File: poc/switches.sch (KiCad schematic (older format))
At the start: 37 parts

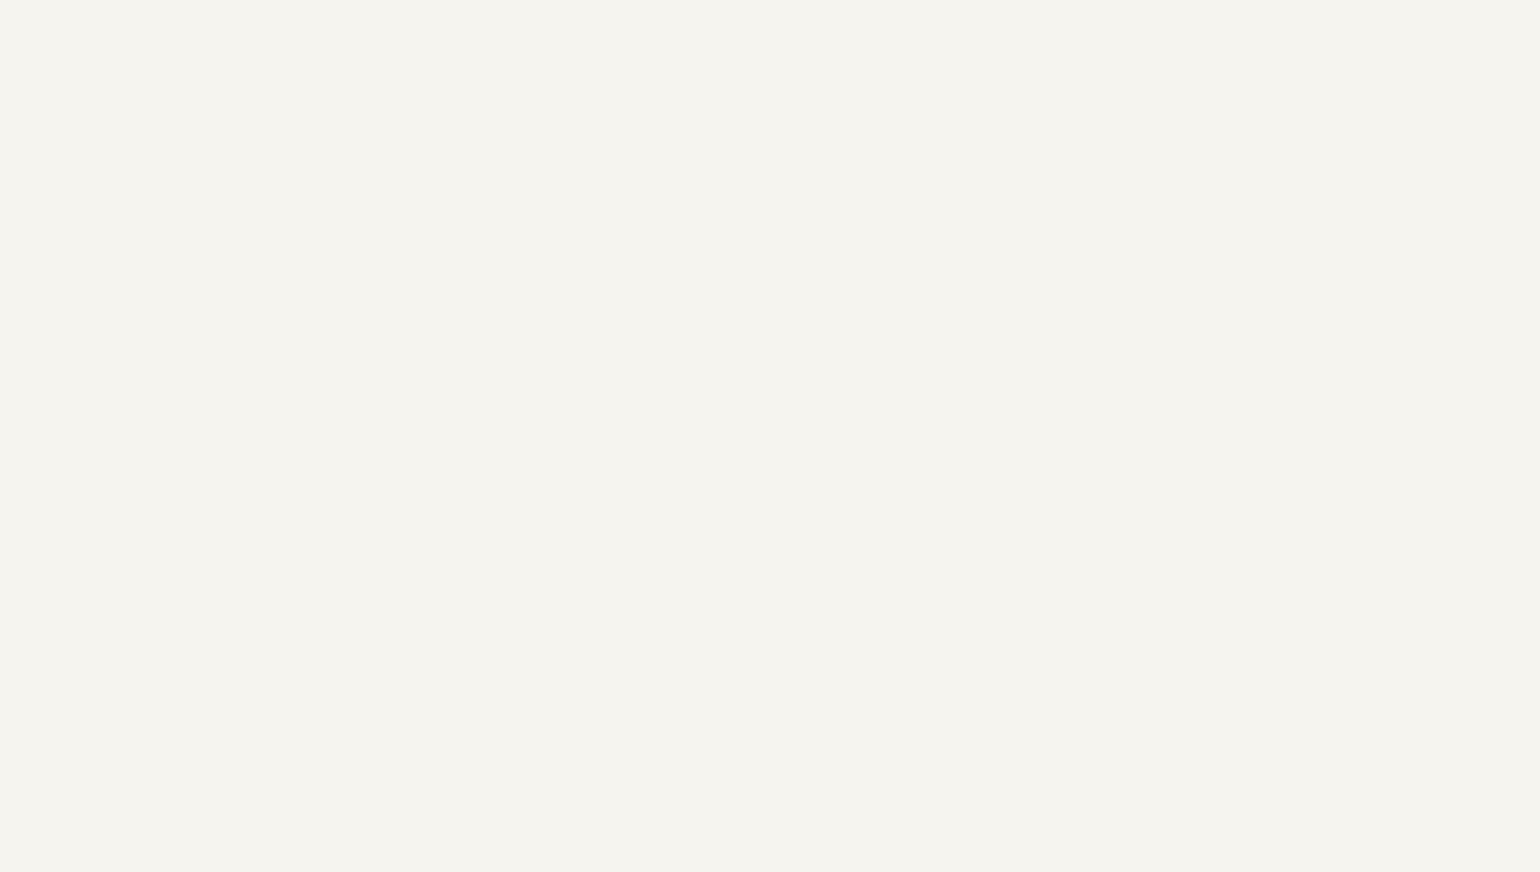
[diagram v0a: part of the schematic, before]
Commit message: Power for a gige phy
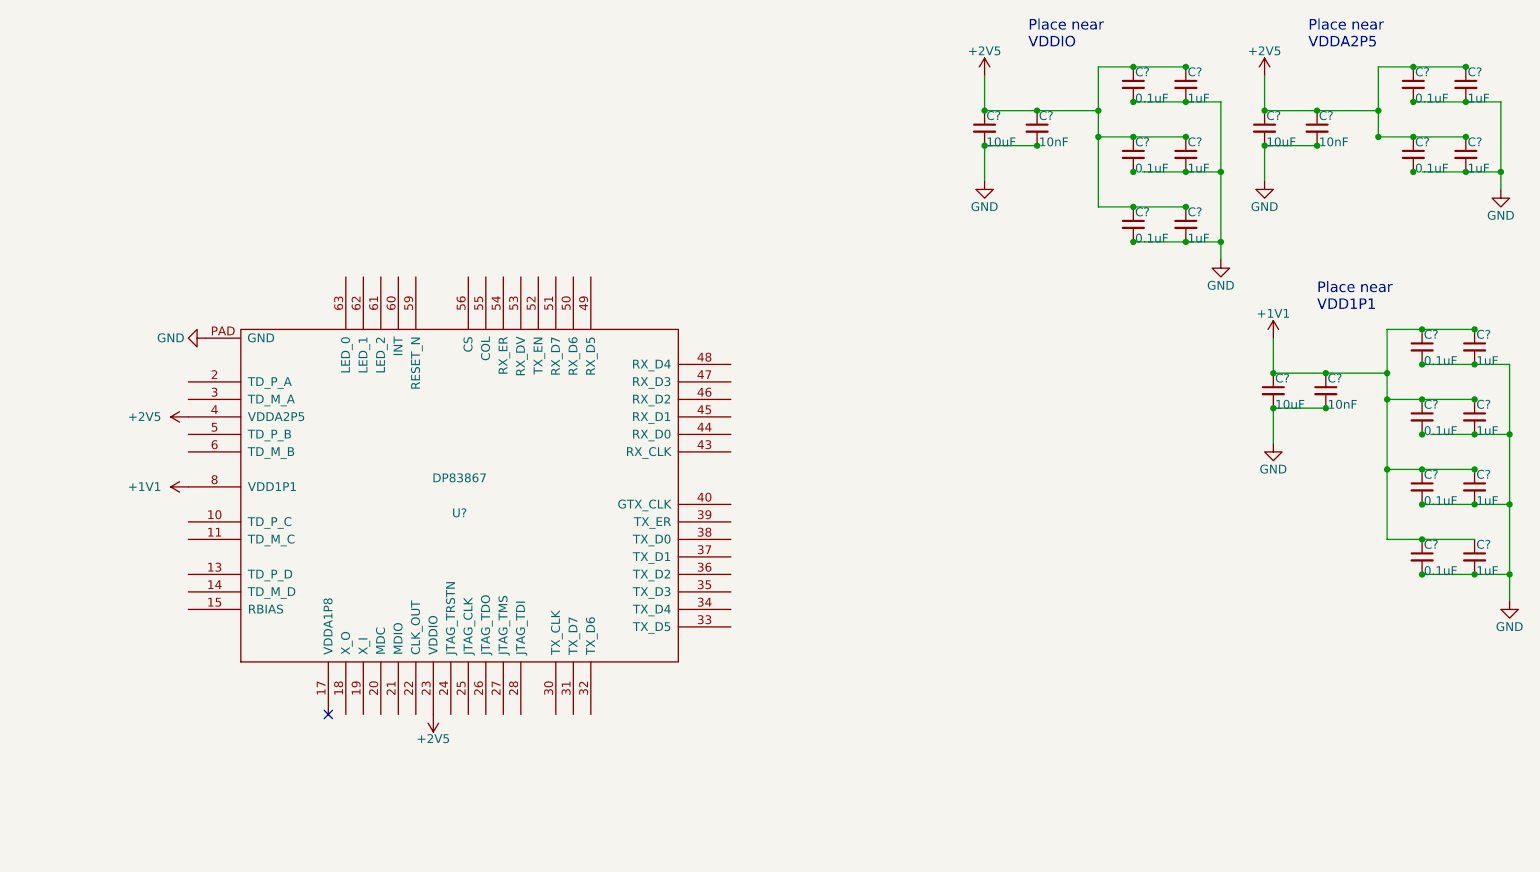
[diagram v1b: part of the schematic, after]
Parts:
- added C? (x3): 10uF, symbol C_Small
- added C? (x3): 10nF, symbol C_Small
- added C? (x9): 0.1uF, symbol C_Small
- added C? (x9): 1uF, symbol C_Small
- added U?: DP83867, MODULE, symbol DP83867
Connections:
- net labels added: +1V1
- wire segments 13 -> 49
- no-connect marks 0 -> 1
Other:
- note added: "Place near\nVDD1P1"
- note added: "Place near\nVDDA2P5"

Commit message: Further organize pi schematics; power for each chip is done!
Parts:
- added C? (x4): 0.1uF, symbol C_Small
- added R?: Belfuse_GigE, symbol Belfuse_GigE
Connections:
- wire segments 49 -> 59
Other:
- note added: "VDDA1P8 is NC\nin two power\nsupply mode"
- moved on the sheet: S?, U?
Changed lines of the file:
@@
 $Descr C 22000 17000
 encoding utf-8
-Sheet 3 3
+Sheet 2 4
 Title ""
 Date ""
@@
 L KSZ9897R S?
 U 1 1 5990AEA3
-P 7000 7250
-F 0 "S?" H 7000 7150 50  0000 C CNN
-F 1 "KSZ9897R" H 7000 7350 50  0000 C CNN
-F 2 "MODULE" H 7000 7250 50  0001 C CNN
-F 3 "DOCUMENTATION" H 7000 7250 50  0001 C CNN
-	1    7000 7250
+P 6950 7250
+F 0 "S?" H 6950 7150 50  0000 C CNN
+F 1 "KSZ9897R" H 6950 7350 50  0000 C CNN
+F 2 "MODULE" H 6950 7250 50  0001 C CNN
+F 3 "DOCUMENTATION" H 6950 7250 50  0001 C CNN
+	1    6950 7250
 	1    0    0    -1
 $EndComp
@@
 L +2V5 #PWR?
 U 1 1 5990AEB1
-P 6350 9500
-F 0 "#PWR?" H 6350 9350 50  0001 C CNN
-F 1 "+2V5" H 6350 9640 50  0000 C CNN
-F 2 "" H 6350 9500 50  0001 C CNN
-F 3 "" H 6350 9500 50  0001 C CNN
-	1    6350 9500
+P 6300 9500
+F 0 "#PWR?" H 6300 9350 50  0001 C CNN
+F 1 "+2V5" H 6300 9640 50  0000 C CNN
+F 2 "" H 6300 9500 50  0001 C CNN
+F 3 "" H 6300 9500 50  0001 C CNN
+	1    6300 9500
 	-1   0    0    1
 $EndComp
@@
 L +1V2 #PWR?
 U 1 1 5990AEB7
-P 5650 9400
-F 0 "#PWR?" H 5650 9250 50  0001 C CNN
-F 1 "+1V2" H 5650 9540 50  0000 C CNN
-F 2 "" H 5650 9400 50  0001 C CNN
-F 3 "" H 5650 9400 50  0001 C CNN
-	1    5650 9400
+P 5600 9400
+F 0 "#PWR?" H 5600 9250 50  0001 C CNN
+F 1 "+1V2" H 5600 9540 50  0000 C CNN
+F 2 "" H 5600 9400 50  0001 C CNN
+F 3 "" H 5600 9400 50  0001 C CNN
+	1    5600 9400
 	-1   0    0    1
 $EndComp
@@
 L +1V2 #PWR?
 U 1 1 5990AEBD
-P 6450 9400
-F 0 "#PWR?" H 6450 9250 50  0001 C CNN
-F 1 "+1V2" H 6450 9540 50  0000 C CNN
-F 2 "" H 6450 9400 50  0001 C CNN
-F 3 "" H 6450 9400 50  0001 C CNN
-	1    6450 9400
+P 6400 9400
+F 0 "#PWR?" H 6400 9250 50  0001 C CNN
+F 1 "+1V2" H 6400 9540 50  0000 C CNN
+F 2 "" H 6400 9400 50  0001 C CNN
+F 3 "" H 6400 9400 50  0001 C CNN
+	1    6400 9400
 	-1   0    0    1
 $EndComp
 Wire Wire Line
-	6350 9400 6350 9500
+	6300 9400 6300 9500
 $Comp
 L +2V5 #PWR?
 U 1 1 5990AEC4
-P 9350 5900
-F 0 "#PWR?" H 9350 5750 50  0001 C CNN
-F 1 "+2V5" V 9350 6100 50  0000 C CNN
-F 2 "" H 9350 5900 50  0001 C CNN
-F 3 "" H 9350 5900 50  0001 C CNN
-	1    9350 5900
+P 9300 5900
+F 0 "#PWR?" H 9300 5750 50  0001 C CNN
+F 1 "+2V5" V 9300 6100 50  0000 C CNN
+F 2 "" H 9300 5900 50  0001 C CNN
+F 3 "" H 9300 5900 50  0001 C CNN
+	1    9300 5900
 	0    1    1    0
 $EndComp
@@
 L GND #PWR?
 U 1 1 5990AECA
-P 9350 7400
-F 0 "#PWR?" H 9350 7150 50  0001 C CNN
-F 1 "GND" V 9350 7200 50  0000 C CNN
-F 2 "" H 9350 7400 50  0001 C CNN
-F 3 "" H 9350 7400 50  0001 C CNN
-	1    9350 7400
+P 9300 7400
+F 0 "#PWR?" H 9300 7150 50  0001 C CNN
+F 1 "GND" V 9300 7200 50  0000 C CNN
+F 2 "" H 9300 7400 50  0001 C CNN
+F 3 "" H 9300 7400 50  0001 C CNN
+	1    9300 7400
 	0    -1   -1   0
 $EndComp
@@
 L DP83867 U?
 U 1 1 599194AF
-P 15400 3250
-F 0 "U?" H 15400 3150 50  0000 C CNN
-F 1 "DP83867" H 15400 3350 50  0000 C CNN
-F 2 "MODULE" H 15400 3250 50  0001 C CNN
-F 3 "DOCUMENTATION" H 15400 3250 50  0001 C CNN
-	1    15400 3250
+P 13400 3200
+F 0 "U?" H 13400 3100 50  0000 C CNN
+F 1 "DP83867" H 13400 3300 50  0000 C CNN
+F 2 "MODULE" H 13400 3200 50  0001 C CNN
+F 3 "DOCUMENTATION" H 13400 3200 50  0001 C CNN
+	1    13400 3200
 	1    0    0    -1
 $EndComp
@@
 L +2V5 #PWR?
 U 1 1 5992229E
-P 15250 4500
-F 0 "#PWR?" H 15250 4350 50  0001 C CNN
-F 1 "+2V5" H 15250 4640 50  0000 C CNN
-F 2 "" H 15250 4500 50  0001 C CNN
-F 3 "" H 15250 4500 50  0001 C CNN
-	1    15250 4500
+P 13250 4450
+F 0 "#PWR?" H 13250 4300 50  0001 C CNN
+F 1 "+2V5" H 13250 4590 50  0000 C CNN
+F 2 "" H 13250 4450 50  0001 C CNN
+F 3 "" H 13250 4450 50  0001 C CNN
+	1    13250 4450
 	-1   0    0    1
 $EndComp
-NoConn ~ 14650 4500
+NoConn ~ 12650 4450
 $Comp
 L GND #PWR?
 U 1 1 59924BE1
-P 13950 2350
-F 0 "#PWR?" H 13950 2100 50  0001 C CNN
-F 1 "GND" V 13950 2150 50  0000 C CNN
-F 2 "" H 13950 2350 50  0001 C CNN
-F 3 "" H 13950 2350 50  0001 C CNN
-	1    13950 2350
+P 11950 2300
+F 0 "#PWR?" H 11950 2050 50  0001 C CNN
+F 1 "GND" V 11950 2100 50  0000 C CNN
+F 2 "" H 11950 2300 50  0001 C CNN
+F 3 "" H 11950 2300 50  0001 C CNN
+	1    11950 2300
 	0    1    1    0
 $EndComp
@@
 L +2V5 #PWR?
 U 1 1 5992579B
-P 13850 2800
-F 0 "#PWR?" H 13850 2650 50  0001 C CNN
-F 1 "+2V5" V 13850 3050 50  0000 C CNN
-F 2 "" H 13850 2800 50  0001 C CNN
-F 3 "" H 13850 2800 50  0001 C CNN
-	1    13850 2800
+P 11850 2750
+F 0 "#PWR?" H 11850 2600 50  0001 C CNN
+F 1 "+2V5" V 11850 3000 50  0000 C CNN
+F 2 "" H 11850 2750 50  0001 C CNN
+F 3 "" H 11850 2750 50  0001 C CNN
+	1    11850 2750
 	0    -1   -1   0
 $EndComp
@@
 L +1V1 #PWR?
 U 1 1 5992648B
-P 13850 3200
-F 0 "#PWR?" H 13850 3050 50  0001 C CNN
-F 1 "+1V1" V 13850 3450 50  0000 C CNN
-F 2 "" H 13850 3200 50  0001 C CNN
-F 3 "" H 13850 3200 50  0001 C CNN
-	1    13850 3200
+P 11850 3150
+F 0 "#PWR?" H 11850 3000 50  0001 C CNN
+F 1 "+1V1" V 11850 3400 50  0000 C CNN
+F 2 "" H 11850 3150 50  0001 C CNN
+F 3 "" H 11850 3150 50  0001 C CNN
+	1    11850 3150
 	0    -1   -1   0
 $EndComp
+Text Notes 11950 4450 0    60   ~ 0
+VDDA1P8 is NC\nin two power\nsupply mode
+$Comp
+L Belfuse_GigE R?
+U 1 1 5991DB72
+P 18500 2450
+F 0 "R?" H 18600 2250 60  0000 C CNN
+F 1 "Belfuse_GigE" H 18500 2400 60  0000 C CNN
+F 2 "" H 18500 2450 60  0001 C CNN
+F 3 "" H 18500 2450 60  0001 C CNN
+	1    18500 2450
+	1    0    0    -1
+$EndComp
+$Comp
+L GND #PWR?
+U 1 1 5991E37F
+P 19100 3450
+F 0 "#PWR?" H 19100 3200 50  0001 C CNN
+F 1 "GND" H 19100 3300 50  0000 C CNN
+F 2 "" H 19100 3450 50  0001 C CNN
+F 3 "" H 19100 3450 50  0001 C CNN
+	1    19100 3450
+	1    0    0    -1
+$EndComp
+$Comp
+L GND #PWR?
+U 1 1 5991E48D
+P 17100 4400
+F 0 "#PWR?" H 17100 4150 50  0001 C CNN
+F 1 "GND" H 17100 4250 50  0000 C CNN
+F 2 "" H 17100 4400 50  0001 C CNN
+F 3 "" H 17100 4400 50  0001 C CNN
+	1    17100 4400
+	1    0    0    -1
+$EndComp
+$Comp
+L C_Small C?
+U 1 1 5991EA82
+P 16600 4200
+F 0 "C?" H 16610 4270 50  0000 L CNN
+F 1 "0.1uF" H 16610 4120 50  0000 L CNN
+F 2 "" H 16600 4200 50  0001 C CNN
+F 3 "" H 16600 4200 50  0001 C CNN
+	1    16600 4200
+	1    0    0    -1
+$EndComp
+$Comp
+L C_Small C?
+U 1 1 5991EFFF
+P 16900 4200
+F 0 "C?" H 16910 4270 50  0000 L CNN
+F 1 "0.1uF" H 16910 4120 50  0000 L CNN
+F 2 "" H 16900 4200 50  0001 C CNN
+F 3 "" H 16900 4200 50  0001 C CNN
+	1    16900 4200
+	1    0    0    -1
+$EndComp
+$Comp
+L C_Small C?
+U 1 1 5991F0DE
+P 17200 4200
+F 0 "C?" H 17210 4270 50  0000 L CNN
+F 1 "0.1uF" H 17210 4120 50  0000 L CNN
+F 2 "" H 17200 4200 50  0001 C CNN
+F 3 "" H 17200 4200 50  0001 C CNN
+	1    17200 4200
+	1    0    0    -1
+$EndComp
+$Comp
+L C_Small C?
+U 1 1 5991F1C0
+P 17500 4200
+F 0 "C?" H 17510 4270 50  0000 L CNN
+F 1 "0.1uF" H 17510 4120 50  0000 L CNN
+F 2 "" H 17500 4200 50  0001 C CNN
+F 3 "" H 17500 4200 50  0001 C CNN
+	1    17500 4200
+	1    0    0    -1
+$EndComp
+Wire Wire Line
+	16600 4300 17500 4300
+Wire Wire Line
+	17100 4300 17100 4400
+Connection ~ 17100 4300
+Connection ~ 16900 4300
+Connection ~ 17200 4300
+Wire Wire Line
+	17900 3800 17500 3800
+Wire Wire Line
+	17500 3800 17500 4100
+Wire Wire Line
+	17900 3450 17200 3450
+Wire Wire Line
+	17200 3450 17200 4100
+Wire Wire Line
+	17900 3100 16900 3100
+Wire Wire Line
+	16900 3100 16900 4100
+Wire Wire Line
+	17900 2750 16600 2750
+Wire Wire Line
+	16600 2750 16600 4100
 $EndSCHEMATC

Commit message: Upgrade to newer kicad
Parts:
- C? (x60): symbol C_Small -> poc-rescue:C_Small
- L? (x4): symbol L_Core_Ferrite -> poc-rescue:L_Core_Ferrite
- R?: symbol Belfuse_GigE -> belfuse_gige:Belfuse_GigE
- S?: symbol KSZ9897R -> KSZ9897R:KSZ9897R
- U?: symbol DP83867 -> DP83867:DP83867

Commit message: wire SD card to cm3l
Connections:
- wire segments 59 -> 151
